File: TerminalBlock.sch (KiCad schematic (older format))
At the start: 7 parts, among them P4 12-pin Terminal Block, P5 3-pin TB

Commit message: Back-annotated footprints into the schematic
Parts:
- C26, C27, C28, C29: footprint (none) -> Capacitors_SMD:c_1210
- P4: footprint (none) -> BenchBudEE:12pinTB
- P5: footprint (none) -> BenchBudEE:3pinTB
- R56: footprint (none) -> SMD_Packages:SM0805
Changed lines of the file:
@@
 F 0 "P4" V 6050 1850 60  0000 C CNN
 F 1 "12-pin Terminal Block" V 6150 1850 60  0000 C CNN
-F 2 "" H 6100 1850 60  0000 C CNN
+F 2 "BenchBudEE:12pinTB" H 6100 1850 60  0001 C CNN
 F 3 "" H 6100 1850 60  0000 C CNN
 F 4 "On Shore" H 6100 1850 60  0001 C CNN "MFG Name"
@@
 F 0 "P5" V 4300 3900 50  0000 C CNN
 F 1 "3-pin TB" V 4400 3900 40  0000 C CNN
-F 2 "" H 4350 3900 60  0000 C CNN
+F 2 "BenchBudEE:3pinTB" H 4350 3900 60  0001 C CNN
 F 3 "" H 4350 3900 60  0000 C CNN
 F 4 "Phoenix" H 4350 3900 60  0001 C CNN "MFG Name"
@@
 F 0 "R56" V 3830 2950 40  0000 C CNN
 F 1 "0" V 3757 2951 40  0000 C CNN
-F 2 "" V 3680 2950 30  0000 C CNN
+F 2 "SMD_Packages:SM0805" V 3680 2950 30  0001 C CNN
 F 3 "" H 3750 2950 30  0000 C CNN
 	1    3750 2950
@@
 F 0 "C26" H 4100 3050 40  0000 L CNN
 F 1 "10u" H 4106 2865 40  0000 L CNN
-F 2 "" H 4138 2800 30  0000 C CNN
+F 2 "Capacitors_SMD:c_1210" H 4138 2800 30  0001 C CNN
 F 3 "" H 4100 2950 60  0000 C CNN
 	1    4100 2950
@@
 F 0 "C27" H 4400 3050 40  0000 L CNN
 F 1 "10u" H 4406 2865 40  0000 L CNN
-F 2 "" H 4438 2800 30  0000 C CNN
+F 2 "Capacitors_SMD:c_1210" H 4438 2800 30  0001 C CNN
 F 3 "" H 4400 2950 60  0000 C CNN
 	1    4400 2950
@@
 F 0 "C28" H 4700 3050 40  0000 L CNN
 F 1 "10u" H 4706 2865 40  0000 L CNN
-F 2 "" H 4738 2800 30  0000 C CNN
+F 2 "Capacitors_SMD:c_1210" H 4738 2800 30  0001 C CNN
 F 3 "" H 4700 2950 60  0000 C CNN
 	1    4700 2950
@@
 F 0 "C29" H 5000 3050 40  0000 L CNN
 F 1 "10u" H 5006 2865 40  0000 L CNN
-F 2 "" H 5038 2800 30  0000 C CNN
+F 2 "Capacitors_SMD:c_1210" H 5038 2800 30  0001 C CNN
 F 3 "" H 5000 2950 60  0000 C CNN
 	1    5000 2950

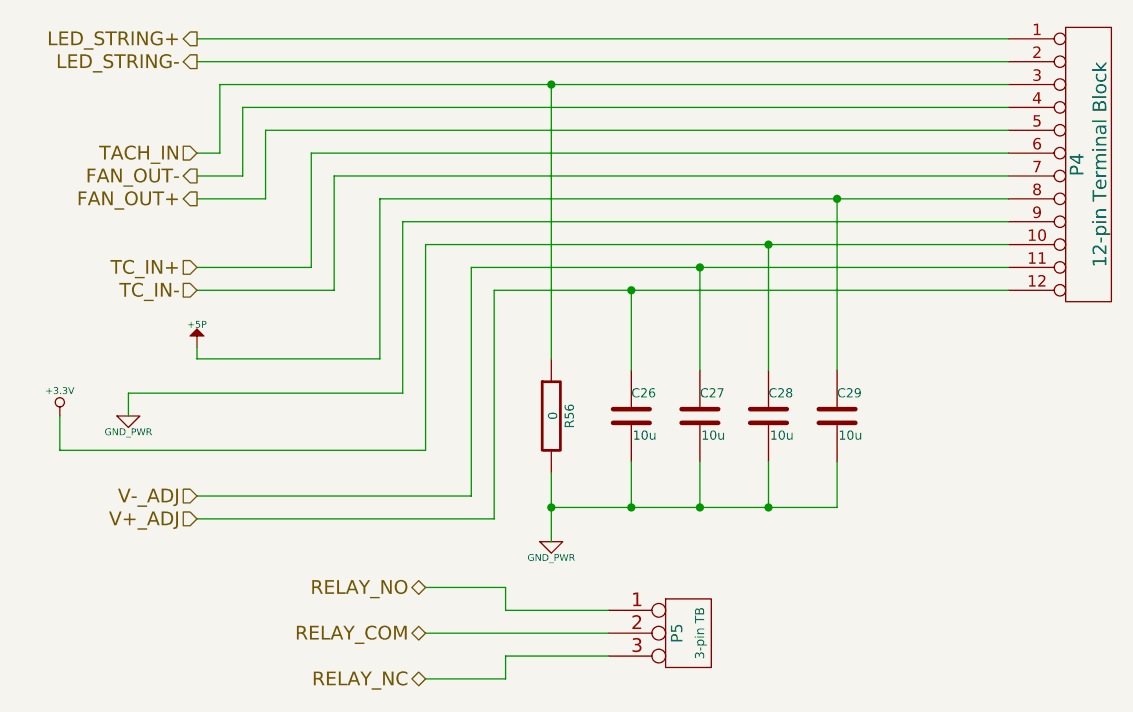
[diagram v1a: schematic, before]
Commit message: Final part numbers added to schematic, cross-checked KiCAD BOM against manual BOM
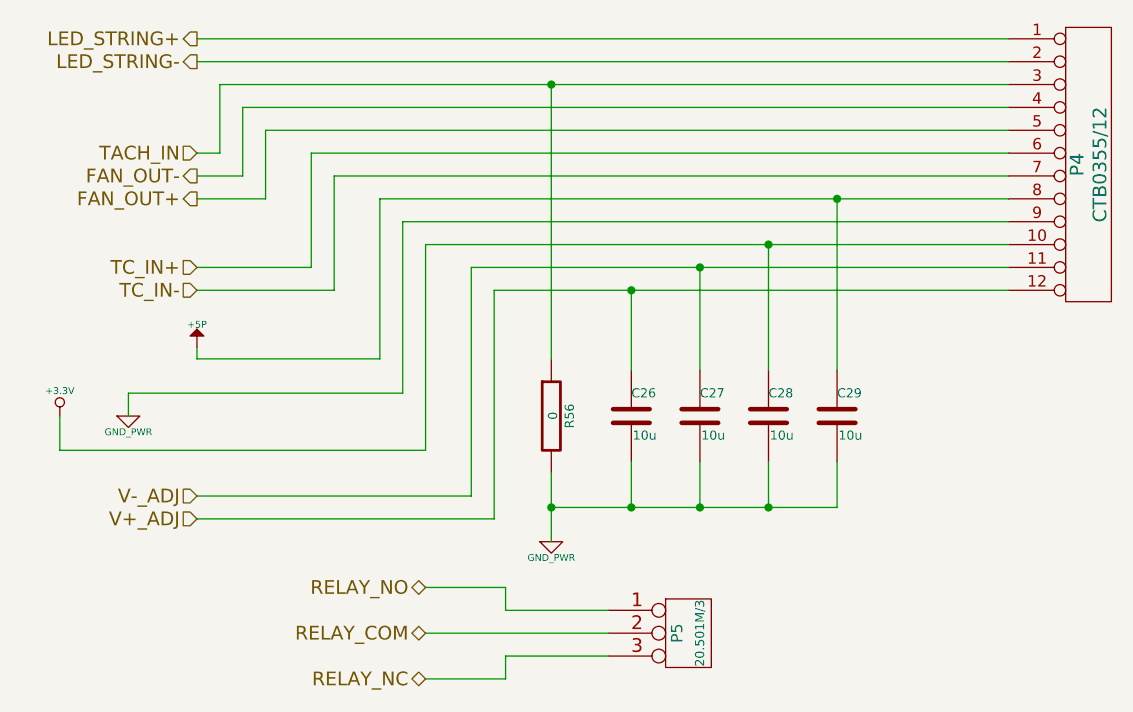
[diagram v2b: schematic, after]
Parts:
- P4: value 12-pin Terminal Block -> CTB0355/12
- P5: value 3-pin TB -> 20.501M/3
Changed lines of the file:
@@
 P 6100 1850
 F 0 "P4" V 6050 1850 60  0000 C CNN
-F 1 "12-pin Terminal Block" V 6150 1850 60  0000 C CNN
+F 1 "CTB0355/12" V 6150 1850 60  0000 C CNN
 F 2 "BenchBudEE:12pinTB" H 6100 1850 60  0001 C CNN
 F 3 "" H 6100 1850 60  0000 C CNN
@@
 P 4350 3900
 F 0 "P5" V 4300 3900 50  0000 C CNN
-F 1 "3-pin TB" V 4400 3900 40  0000 C CNN
+F 1 "20.501M/3" V 4400 3900 40  0000 C CNN
 F 2 "BenchBudEE:3pinTB" H 4350 3900 60  0001 C CNN
 F 3 "" H 4350 3900 60  0000 C CNN
